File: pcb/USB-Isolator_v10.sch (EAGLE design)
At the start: 33 parts, among them IC1 ADUM3160, J1 USB-MICRO, J2 USB-A-AUY1006, U1A RI-0505S, U1B SPU02L-05, X1 PASSER-07, X2 PASSER-07, X3 PASSER-07

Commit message: updated layout and schematics
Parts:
- LOGO3: value LOGO-SPARK_PLACE -> LOGO-S_PLACE_M; device we-symbol:LOGO-SPARK_PLACE -> we-symbol:LOGO-S_PLACE_M
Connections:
- net D+1 renamed D1_P
- net D+2 renamed D2_P
- net D-1 renamed D1_N
- net D-2 renamed D2_N
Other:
- note added: "RECOM RI-0505S or MEANWELL SPU02L-05"
- moved on the sheet: J1, J2
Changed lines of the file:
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@@
 <setting verticaltext="up"/>
 </settings>
-<grid distance="0.1" unitdist="inch" unit="inch" style="lines" multiple="1" display="no" altdistance="0.01" altunitdist="inch" altunit="inch"/>
+<grid distance="0.05" unitdist="inch" unit="inch" style="lines" multiple="1" display="yes" altdistance="0.025" altunitdist="inch" altunit="inch"/>
 <layers>
 <layer number="1" name="Top" color="4" fill="1" visible="no" active="no"/>
@@
 <part name="FRAME1" library="we-symbol" deviceset="FRAME-A4L" device=""/>
 <part name="LOGO2" library="we-symbol" deviceset="OSHW_LOGO" device="X0070"/>
-<part name="LOGO3" library="we-symbol" deviceset="LOGO" device="-SPARK_PLACE"/>
+<part name="LOGO3" library="we-symbol" deviceset="LOGO" device="-S_PLACE_M"/>
 <part name="X1" library="we-symbol" deviceset="PASSER" device="-07"/>
 <part name="X2" library="we-symbol" deviceset="PASSER" device="-07"/>
@@
 <text x="161.29" y="29.21" size="1.27" layer="95">http://creativecommons.org/licenses/by-sa/4.0/</text>
 <text x="161.29" y="25.4" size="1.27" layer="95">Designed by Stephan Watterott (Watterott electronic)</text>
-<text x="107.95" y="88.9" size="3.81" layer="94">DC/DC Converter</text>
+<text x="107.95" y="91.44" size="3.81" layer="94">DC/DC Converter</text>
 <text x="114.3" y="153.67" size="3.81" layer="94">USB Isolator</text>
 <text x="45.72" y="106.68" size="1.778" layer="94" align="top-right">Option 1: RU= 0, CU=NC
@@
 <wire x1="104.14" y1="143.51" x2="106.045" y2="143.51" width="0.8128" layer="94"/>
 <wire x1="153.035" y1="143.51" x2="154.94" y2="143.51" width="0.8128" layer="94"/>
+<text x="110.49" y="88.9" size="1.27" layer="94">RECOM RI-0505S or MEANWELL SPU02L-05</text>
 </plain>
 <instances>
@@
 <wire x1="208.28" y1="124.46" x2="208.28" y2="114.3" width="0.1524" layer="91"/>
 <wire x1="208.28" y1="114.3" x2="208.28" y2="109.22" width="0.1524" layer="91"/>
-<wire x1="208.28" y1="124.46" x2="220.98" y2="124.46" width="0.1524" layer="91"/>
+<wire x1="208.28" y1="124.46" x2="218.44" y2="124.46" width="0.1524" layer="91"/>
 <pinref part="J2" gate="J" pin="GND"/>
 <pinref part="CU2" gate="C" pin="1"/>
@@
 <wire x1="50.8" y1="124.46" x2="50.8" y2="114.3" width="0.1524" layer="91"/>
 <wire x1="50.8" y1="114.3" x2="50.8" y2="109.22" width="0.1524" layer="91"/>
-<wire x1="38.1" y1="124.46" x2="50.8" y2="124.46" width="0.1524" layer="91"/>
+<wire x1="40.64" y1="124.46" x2="50.8" y2="124.46" width="0.1524" layer="91"/>
 <pinref part="J1" gate="J" pin="GND"/>
 <pinref part="RU1" gate="R" pin="2"/>
@@
 </segment>
 </net>
-<net name="D-1" class="0">
-<segment>
-<wire x1="38.1" y1="129.54" x2="62.23" y2="129.54" width="0.1524" layer="91"/>
+<net name="D1_N" class="0">
+<segment>
+<wire x1="40.64" y1="129.54" x2="62.23" y2="129.54" width="0.1524" layer="91"/>
 <pinref part="J1" gate="J" pin="D-"/>
 <pinref part="R1" gate="R" pin="1"/>
@@
 </segment>
 </net>
-<net name="D+1" class="0">
-<segment>
-<wire x1="72.39" y1="132.08" x2="38.1" y2="132.08" width="0.1524" layer="91"/>
+<net name="D1_P" class="0">
+<segment>
+<wire x1="72.39" y1="132.08" x2="40.64" y2="132.08" width="0.1524" layer="91"/>
 <pinref part="J1" gate="J" pin="D+"/>
 <pinref part="R2" gate="R" pin="1"/>
@@
 </segment>
 </net>
-<net name="D+2" class="0">
-<segment>
-<wire x1="220.98" y1="132.08" x2="185.42" y2="132.08" width="0.1524" layer="91"/>
+<net name="D2_P" class="0">
+<segment>
+<wire x1="218.44" y1="132.08" x2="185.42" y2="132.08" width="0.1524" layer="91"/>
 <pinref part="R4" gate="R" pin="2"/>
 <pinref part="J2" gate="J" pin="D+"/>
@@
 </segment>
 </net>
-<net name="D-2" class="0">
+<net name="D2_N" class="0">
 <segment>
 <wire x1="170.18" y1="129.54" x2="195.58" y2="129.54" width="0.1524" layer="91"/>
@@
 <pinref part="J2" gate="J" pin="D-"/>
 <pinref part="D2" gate="D" pin="C2"/>
-<wire x1="195.58" y1="129.54" x2="220.98" y2="129.54" width="0.1524" layer="91"/>
+<wire x1="195.58" y1="129.54" x2="218.44" y2="129.54" width="0.1524" layer="91"/>
 <wire x1="195.58" y1="127" x2="195.58" y2="129.54" width="0.1524" layer="91"/>
 <junction x="195.58" y="129.54"/>
@@
 <segment>
 <wire x1="43.18" y1="134.62" x2="43.18" y2="127" width="0.1524" layer="91"/>
-<wire x1="43.18" y1="127" x2="38.1" y2="127" width="0.1524" layer="91"/>
+<wire x1="43.18" y1="127" x2="40.64" y2="127" width="0.1524" layer="91"/>
 <pinref part="J1" gate="J" pin="VBUS"/>
 <pinref part="F1" gate="F" pin="1"/>
@@
 <pinref part="P+5" gate="G$1" pin="VCC/2"/>
 <wire x1="215.9" y1="140.97" x2="215.9" y2="127" width="0.1524" layer="91"/>
-<wire x1="215.9" y1="127" x2="220.98" y2="127" width="0.1524" layer="91"/>
+<wire x1="215.9" y1="127" x2="218.44" y2="127" width="0.1524" layer="91"/>
 </segment>
 </net>
@@
 <pinref part="J1" gate="J" pin="SHIELD"/>
 <wire x1="35.56" y1="114.3" x2="35.56" y2="118.11" width="0.1524" layer="91"/>
-<wire x1="33.02" y1="119.38" x2="33.02" y2="114.3" width="0.1524" layer="91"/>
+<wire x1="35.56" y1="119.38" x2="33.02" y2="114.3" width="0.1524" layer="91"/>
 <wire x1="33.02" y1="114.3" x2="35.56" y2="114.3" width="0.1524" layer="91"/>
 <junction x="35.56" y="114.3"/>
@@
 <wire x1="223.52" y1="114.3" x2="223.52" y2="118.11" width="0.1524" layer="91"/>
 <wire x1="223.52" y1="114.3" x2="226.06" y2="114.3" width="0.1524" layer="91"/>
-<wire x1="226.06" y1="114.3" x2="226.06" y2="119.38" width="0.1524" layer="91"/>
+<wire x1="226.06" y1="114.3" x2="223.52" y2="119.38" width="0.1524" layer="91"/>
 <junction x="223.52" y="114.3"/>
 </segment>

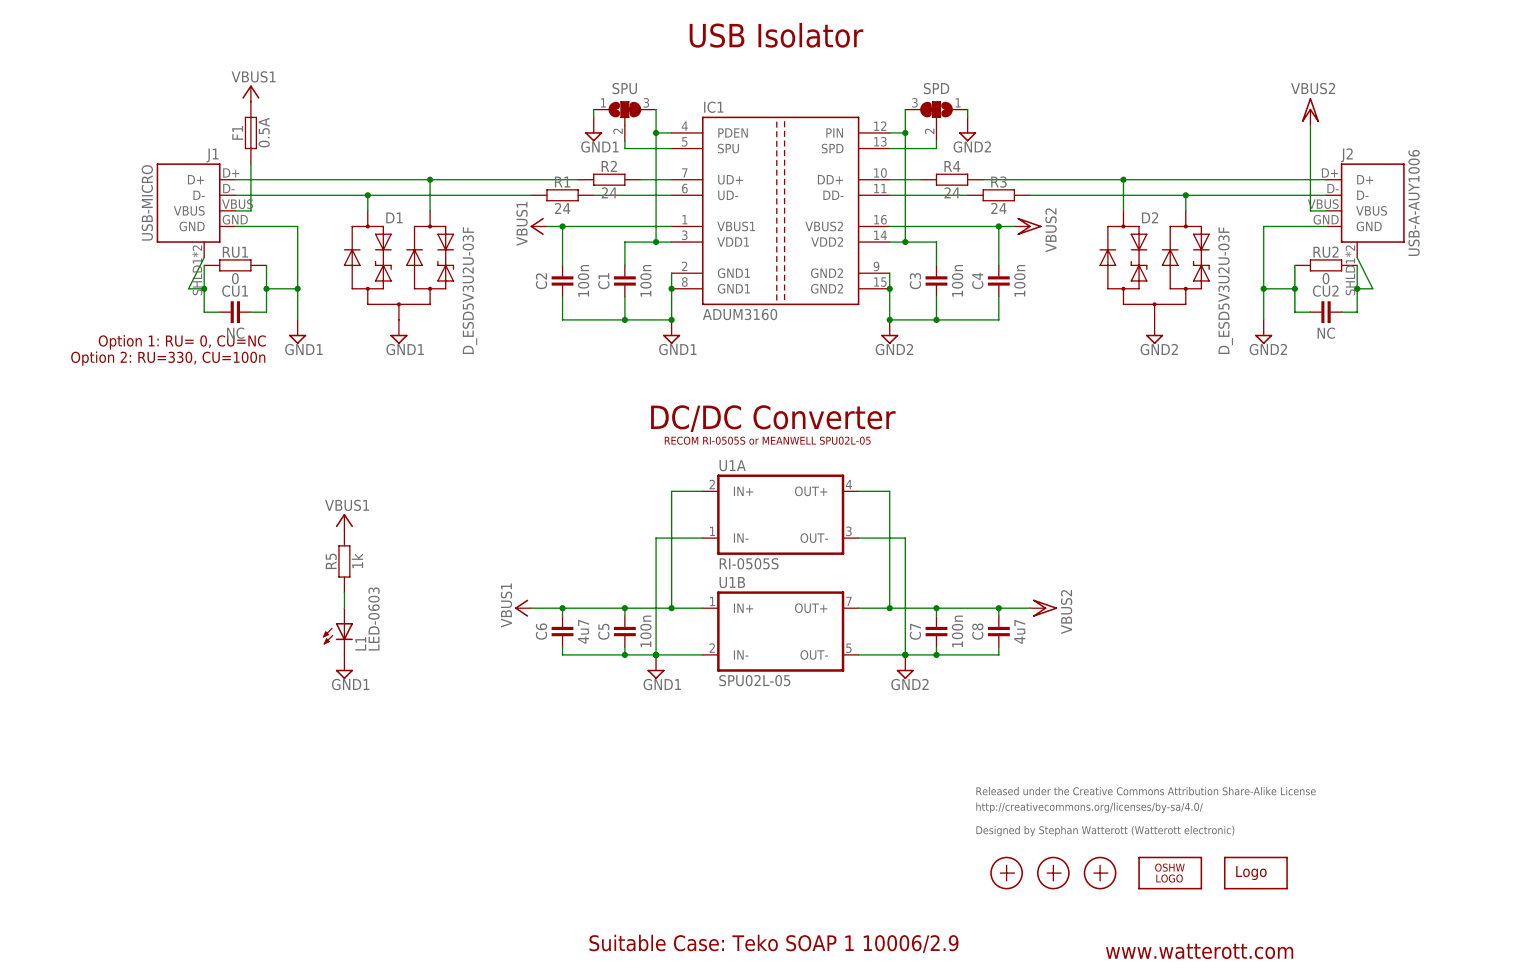
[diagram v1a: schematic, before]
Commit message: updated schematics
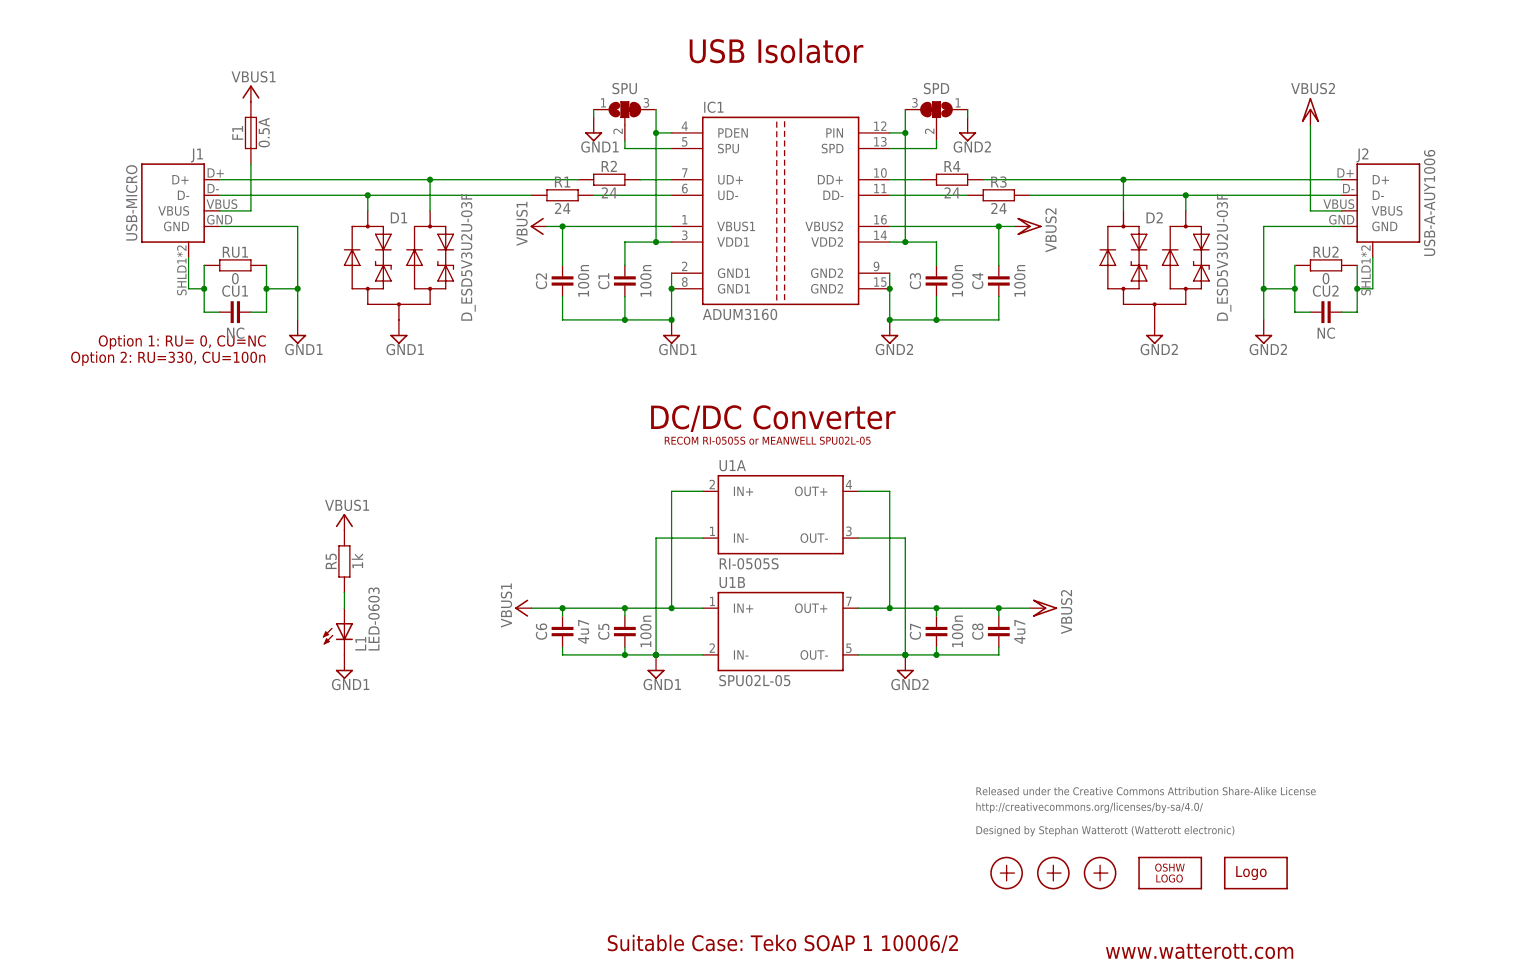
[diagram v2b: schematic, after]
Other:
- note added: "Suitable Case: Teko SOAP 1 10006/2"
- note removed: "Suitable Case: Teko SOAP 1 10006/2.9"
- moved on the sheet: J1, J2
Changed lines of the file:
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@@
 <setting verticaltext="up"/>
 </settings>
-<grid distance="0.05" unitdist="inch" unit="inch" style="lines" multiple="1" display="yes" altdistance="0.025" altunitdist="inch" altunit="inch"/>
+<grid distance="0.1" unitdist="inch" unit="inch" style="lines" multiple="1" display="no" altdistance="0.01" altunitdist="inch" altunit="inch"/>
 <layers>
 <layer number="1" name="Top" color="4" fill="1" visible="no" active="no"/>
@@
 <plain>
 <text x="213.36" y="5.08" size="2.54" layer="94" font="vector" align="bottom-right">www.watterott.com</text>
-<text x="158.75" y="8.89" size="2.54" layer="94" rot="R180">Suitable Case: Teko SOAP 1 10006/2.9</text>
+<text x="158.75" y="8.89" size="2.54" layer="94" rot="R180">Suitable Case: Teko SOAP 1 10006/2</text>
 <text x="161.29" y="31.75" size="1.27" layer="95">Released under the Creative Commons Attribution Share-Alike License</text>
 <text x="161.29" y="29.21" size="1.27" layer="95">http://creativecommons.org/licenses/by-sa/4.0/</text>
 <text x="161.29" y="25.4" size="1.27" layer="95">Designed by Stephan Watterott (Watterott electronic)</text>
 <text x="107.95" y="91.44" size="3.81" layer="94">DC/DC Converter</text>
-<text x="114.3" y="153.67" size="3.81" layer="94">USB Isolator</text>
+<text x="114.3" y="151.13" size="3.81" layer="94">USB Isolator</text>
 <text x="45.72" y="106.68" size="1.778" layer="94" align="top-right">Option 1: RU= 0, CU=NC
 Option 2: RU=330, CU=100n</text>
@@
 <instance part="SUPPLY2" gate="G$1" x="149.86" y="52.07"/>
 <instance part="SUPPLY6" gate="G$1" x="208.28" y="106.68"/>
-<instance part="J1" gate="J" x="33.02" y="127" rot="MR0"/>
+<instance part="J1" gate="J" x="30.48" y="127" rot="MR0"/>
 <instance part="C1" gate="C" x="104.14" y="115.57" rot="R90"/>
 <instance part="C2" gate="C" x="93.98" y="115.57" rot="R90"/>
@@
 <attribute name="VALUE" x="157.48" y="130.81" size="1.778" layer="96" align="top-center"/>
 </instance>
-<instance part="J2" gate="J" x="226.06" y="127"/>
+<instance part="J2" gate="J" x="228.6" y="127"/>
 <instance part="FRAME1" gate="G$1" x="0" y="0"/>
 <instance part="LOGO2" gate="G$1" x="193.04" y="19.05"/>
@@
 <wire x1="208.28" y1="124.46" x2="208.28" y2="114.3" width="0.1524" layer="91"/>
 <wire x1="208.28" y1="114.3" x2="208.28" y2="109.22" width="0.1524" layer="91"/>
-<wire x1="208.28" y1="124.46" x2="218.44" y2="124.46" width="0.1524" layer="91"/>
+<wire x1="208.28" y1="124.46" x2="220.98" y2="124.46" width="0.1524" layer="91"/>
 <pinref part="J2" gate="J" pin="GND"/>
 <pinref part="CU2" gate="C" pin="1"/>
@@
 <wire x1="50.8" y1="124.46" x2="50.8" y2="114.3" width="0.1524" layer="91"/>
 <wire x1="50.8" y1="114.3" x2="50.8" y2="109.22" width="0.1524" layer="91"/>
-<wire x1="40.64" y1="124.46" x2="50.8" y2="124.46" width="0.1524" layer="91"/>
+<wire x1="38.1" y1="124.46" x2="50.8" y2="124.46" width="0.1524" layer="91"/>
 <pinref part="J1" gate="J" pin="GND"/>
 <pinref part="RU1" gate="R" pin="2"/>
@@
 <net name="D1_N" class="0">
 <segment>
-<wire x1="40.64" y1="129.54" x2="62.23" y2="129.54" width="0.1524" layer="91"/>
+<wire x1="38.1" y1="129.54" x2="62.23" y2="129.54" width="0.1524" layer="91"/>
 <pinref part="J1" gate="J" pin="D-"/>
 <pinref part="R1" gate="R" pin="1"/>
@@
 <net name="D1_P" class="0">
 <segment>
-<wire x1="72.39" y1="132.08" x2="40.64" y2="132.08" width="0.1524" layer="91"/>
+<wire x1="72.39" y1="132.08" x2="38.1" y2="132.08" width="0.1524" layer="91"/>
 <pinref part="J1" gate="J" pin="D+"/>
 <pinref part="R2" gate="R" pin="1"/>
@@
 <net name="D2_P" class="0">
 <segment>
-<wire x1="218.44" y1="132.08" x2="185.42" y2="132.08" width="0.1524" layer="91"/>
+<wire x1="220.98" y1="132.08" x2="185.42" y2="132.08" width="0.1524" layer="91"/>
 <pinref part="R4" gate="R" pin="2"/>
 <pinref part="J2" gate="J" pin="D+"/>
@@
 <pinref part="J2" gate="J" pin="D-"/>
 <pinref part="D2" gate="D" pin="C2"/>
-<wire x1="195.58" y1="129.54" x2="218.44" y2="129.54" width="0.1524" layer="91"/>
+<wire x1="195.58" y1="129.54" x2="220.98" y2="129.54" width="0.1524" layer="91"/>
 <wire x1="195.58" y1="127" x2="195.58" y2="129.54" width="0.1524" layer="91"/>
 <junction x="195.58" y="129.54"/>
@@
 <segment>
 <wire x1="43.18" y1="134.62" x2="43.18" y2="127" width="0.1524" layer="91"/>
-<wire x1="43.18" y1="127" x2="40.64" y2="127" width="0.1524" layer="91"/>
+<wire x1="43.18" y1="127" x2="38.1" y2="127" width="0.1524" layer="91"/>
 <pinref part="J1" gate="J" pin="VBUS"/>
 <pinref part="F1" gate="F" pin="1"/>
@@
 <pinref part="P+5" gate="G$1" pin="VCC/2"/>
 <wire x1="215.9" y1="140.97" x2="215.9" y2="127" width="0.1524" layer="91"/>
-<wire x1="215.9" y1="127" x2="218.44" y2="127" width="0.1524" layer="91"/>
+<wire x1="215.9" y1="127" x2="220.98" y2="127" width="0.1524" layer="91"/>
 </segment>
 </net>
@@
 <pinref part="J1" gate="J" pin="SHIELD"/>
 <wire x1="35.56" y1="114.3" x2="35.56" y2="118.11" width="0.1524" layer="91"/>
-<wire x1="35.56" y1="119.38" x2="33.02" y2="114.3" width="0.1524" layer="91"/>
+<wire x1="33.02" y1="119.38" x2="33.02" y2="114.3" width="0.1524" layer="91"/>
 <wire x1="33.02" y1="114.3" x2="35.56" y2="114.3" width="0.1524" layer="91"/>
 <junction x="35.56" y="114.3"/>
@@
 <wire x1="223.52" y1="114.3" x2="223.52" y2="118.11" width="0.1524" layer="91"/>
 <wire x1="223.52" y1="114.3" x2="226.06" y2="114.3" width="0.1524" layer="91"/>
-<wire x1="226.06" y1="114.3" x2="223.52" y2="119.38" width="0.1524" layer="91"/>
+<wire x1="226.06" y1="114.3" x2="226.06" y2="119.38" width="0.1524" layer="91"/>
 <junction x="223.52" y="114.3"/>
 </segment>
